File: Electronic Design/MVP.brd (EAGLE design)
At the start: 91.3 x 85.8 mm, 38 parts, among them IC1 ACS711KLCTR-12AB-T, IC3 ATMEGA328-PU, Q2 16MHz, Q3 IRF9540, Q4 IRF9540

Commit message: adding trace for pin16 on atmega to go to jumper
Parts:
- moved C3 46.4 mm to (78.5, 54.5), turned to 270 degrees
- moved C4 12.1 mm to (39.2, 42.5), turned to 270 degrees
- moved JP1 1.99 mm to (81.6, 44.9)
- moved Q2 1.99 mm to (85.2, 62.2)
- moved R1 1.99 mm to (73.5, 31.9)
- moved R5 1.99 mm to (79.5, 74.7)
- moved C13 1.99 mm to (85.3, 34.5)
- moved C20 1.99 mm to (78.5, 59.9)
- moved R3 1.99 mm to (44.6, 39.8)
- moved VIN_BUCK 1.99 mm to (76.1, 24.7)
- moved F1 1.99 mm to (29.0, 73.3)
- moved R12 1.99 mm to (18.6, 54.2)
- moved R14 1.99 mm to (30.7, 42.7)
- moved S1 1.99 mm to (28.9, 13.0)
- moved VIN 1.99 mm to (5.75, 70.2)
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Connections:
- net N$9: now also IC3.16
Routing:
- net +5V: track 119.3 -> 97.7 mm
- net GND: track 10.2 -> 0.00 mm
- net N$9: track 0.00 -> 8.11 mm
- net +3V3: track 106.3 -> 99.4 mm
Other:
- board size 91.3 x 85.8 mm -> 94.3 x 85.7 mm
- board text removed: "5V"
- board text removed: "GND"
- board text removed: "IIN1"
- board text removed: "VIN1"

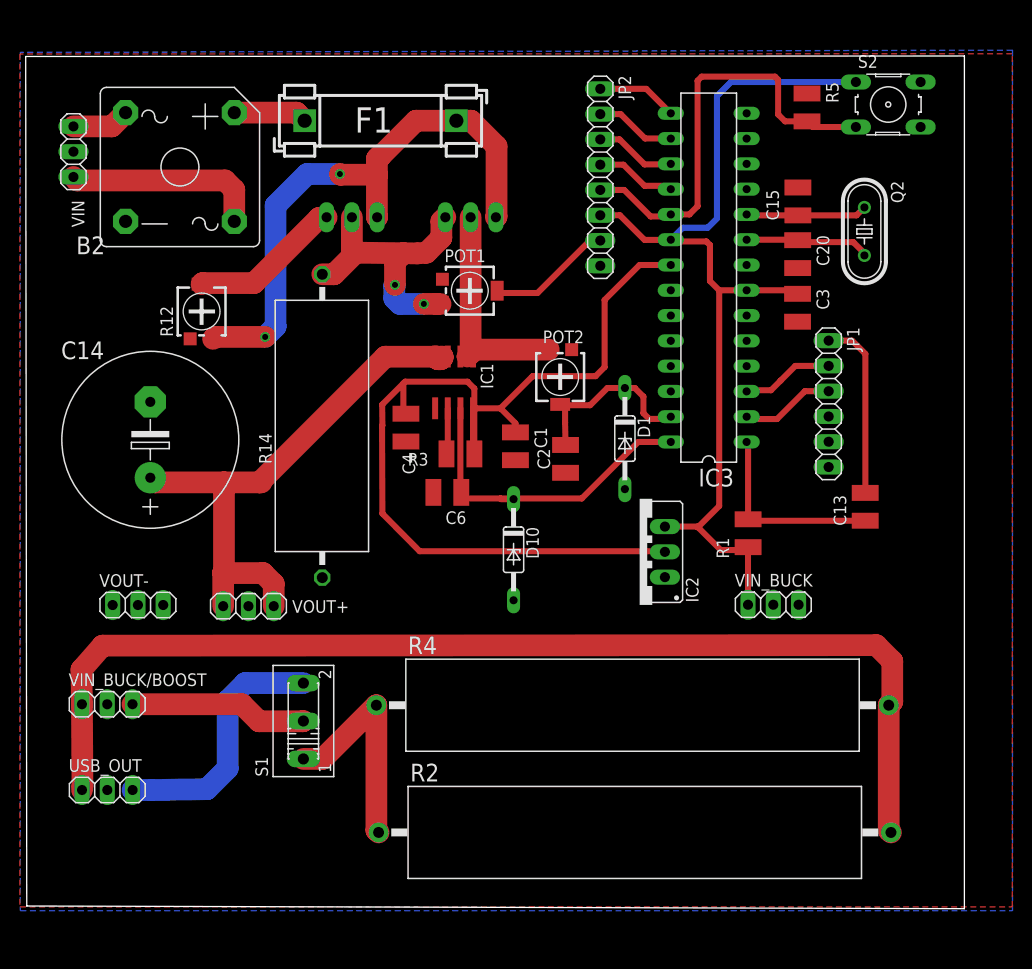
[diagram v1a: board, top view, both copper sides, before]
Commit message: Change some components connections in schematics and update board layout
changed top and bottom layer isolation to 0.3
completed unrouted wires
rerouted Output to come from capacitor directly
moved +3V3 near POT2 to allow more space forground trace to penetrate to C1 and C2
moved decoupling caps C4 and C1 closer to IC1 and IC3, respectively
added several ground stitching vias between top and bottom layer
increased some corner sizes
rerouted +5V from under IC4 to go through decoupling cap C3
connected R5 to GND
connected JP1 to GND
mirrored POT1 to allow easier routing
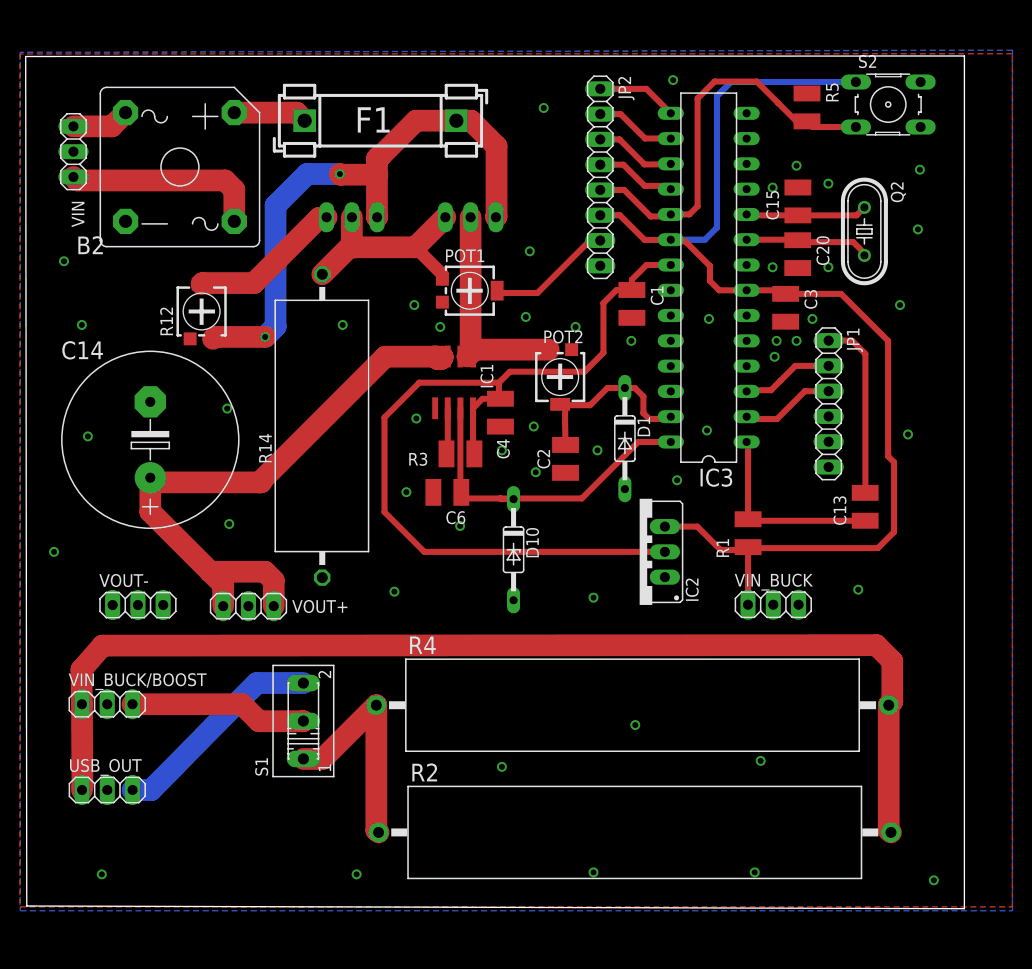
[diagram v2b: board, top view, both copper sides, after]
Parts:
- moved C1 18.5 mm to (61.9, 54.9)
- moved C4 9.62 mm to (48.7, 44.0)
- moved C3 1.20 mm to (77.3, 54.5)
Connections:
- removed net N$21: JP1.6
- removed net N$26: R5.1
- net GND: now also JP1.6, POT1.3, R5.1; no longer POT1.1
- net N$35: now also POT1.1; no longer POT1.3
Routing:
- net +5V: track 97.7 -> 118.1 mm
- net +3V3: track 99.4 -> 87.5 mm
- net N$35: track 29.2 -> 22.1 mm, vias 2 -> 0
- net M1S: track 56.6 -> 62.1 mm
- net N$25: track 25.6 -> 21.7 mm
- net N$8: track 44.1 -> 40.6 mm
- net IIN: track 31.9 -> 33.5 mm
- net VIN: track 18.0 -> 18.6 mm

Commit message: moved VOUT+, USB_OUT, VIN_BUCK/BOOST and VIN_BUCK closer to the edges as these will most likely be replaced with screw terminals (I couldn't find the component for these in eagle)
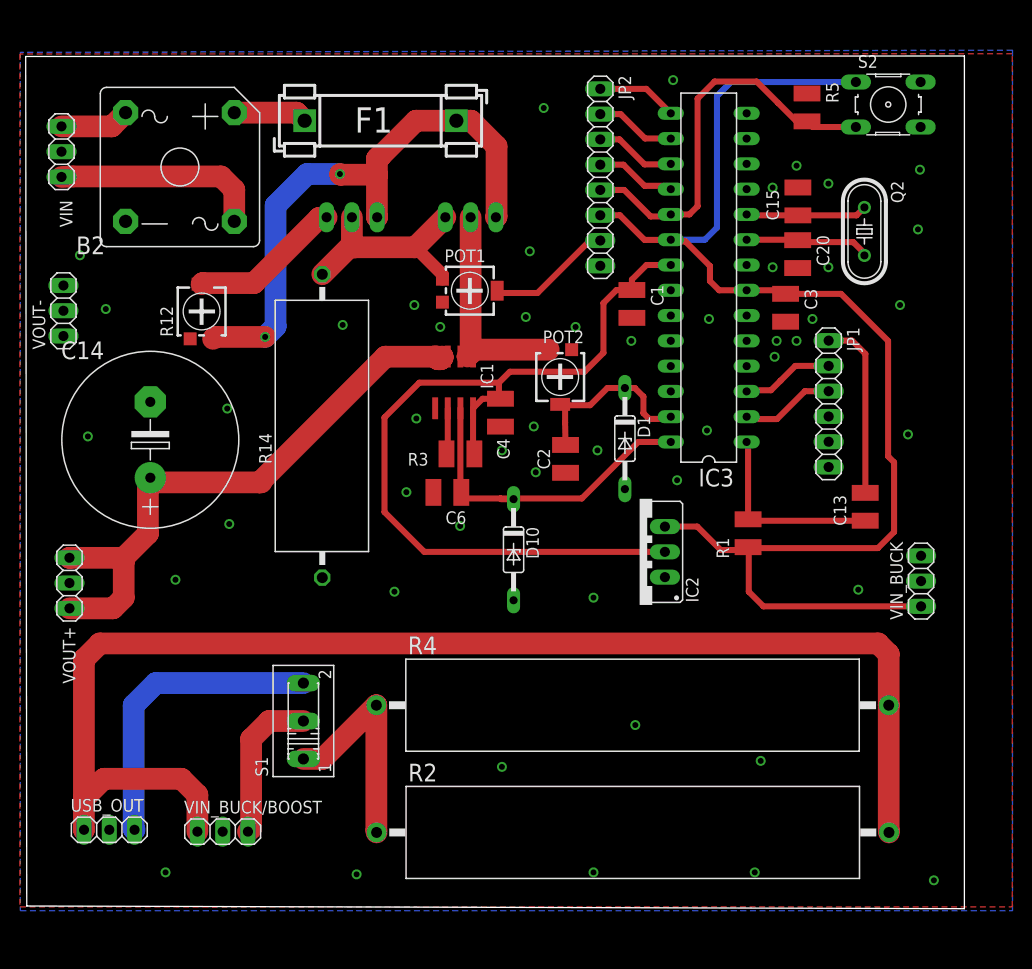
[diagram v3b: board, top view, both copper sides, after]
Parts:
- moved VOUT- 30.5 mm to (4.74, 54.2), turned to 90 degrees
- moved VOUT+ 18.1 mm to (5.35, 26.9), turned to 270 degrees
- moved VIN_BUCK/BOOST 17.3 mm to (20.7, 1.89)
- moved VIN_BUCK 15.0 mm to (90.9, 27.1), turned to 90 degrees
- moved USB_OUT 4.00 mm to (9.35, 2.07)
- moved VIN 1.20 mm to (4.55, 70.2)
- moved R2 0.20 mm to (61.9, 1.81)
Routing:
- net N$23: track 112.8 -> 133.6 mm
- net +5V: track 118.1 -> 134.7 mm
- net N$25: track 21.7 -> 30.5 mm
- net N$22: track 17.9 -> 15.4 mm
- net N$19: track 19.9 -> 21.1 mm
- net N$20: track 5.81 -> 7.01 mm
- net M1S: track 62.1 -> 61.2 mm

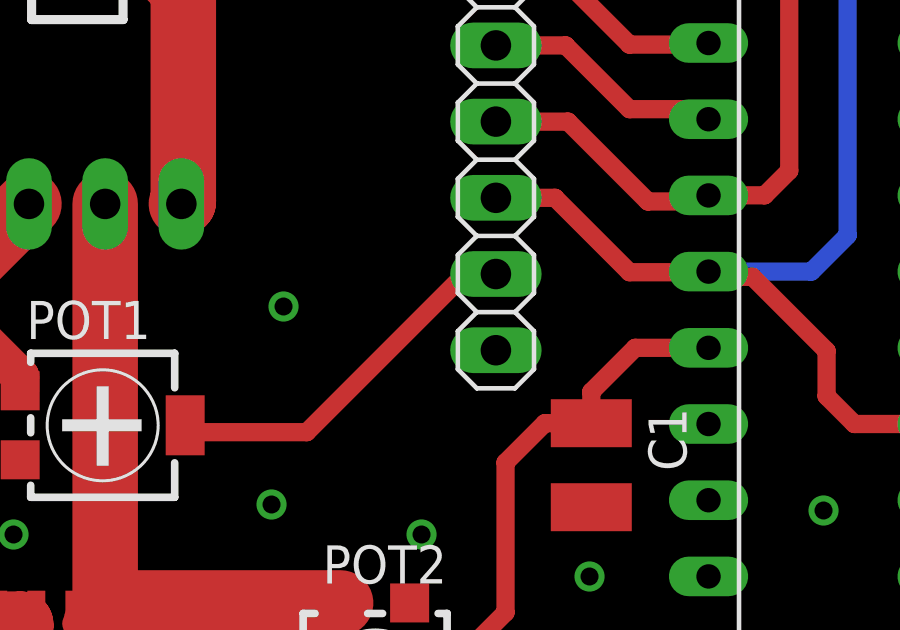
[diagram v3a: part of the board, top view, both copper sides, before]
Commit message: Changed position of 5V and overvoltage on JP2
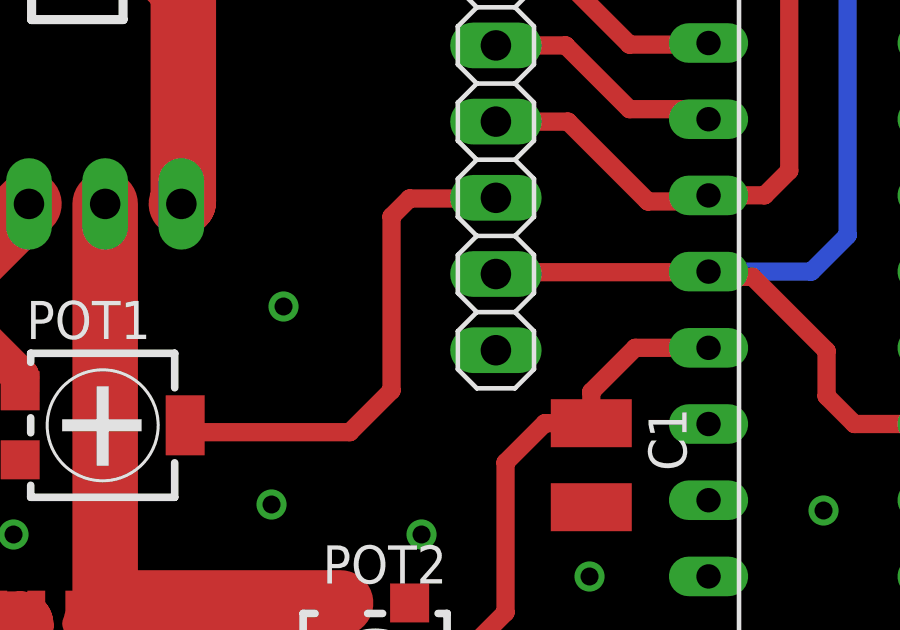
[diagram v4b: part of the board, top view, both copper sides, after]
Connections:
- net +5V: now also JP2.7; no longer JP2.6
- net OVERV: now also JP2.6; no longer JP2.7
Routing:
- net OVERV: track 12.6 -> 17.1 mm
- net +5V: track 134.7 -> 133.7 mm
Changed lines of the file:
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@@
 <wire x1="73.435846875" y1="30.3795" x2="73.532515625" y2="30.47616875" width="0.6096" layer="1"/>
 <contactref element="S2" pad="1"/>
-<contactref element="JP2" pad="6"/>
-<wire x1="58.67934375" y1="63.82278125" x2="60.65080625" y2="63.82278125" width="0.6096" layer="1"/>
-<wire x1="60.65080625" y1="63.82278125" x2="63.1309125" y2="61.342675" width="0.6096" layer="1"/>
-<wire x1="63.1309125" y1="61.342675" x2="65.746790625" y2="61.342675" width="0.6096" layer="1"/>
 <wire x1="65.746790625" y1="61.342675" x2="65.76684375" y2="61.362728125" width="0.6096" layer="1"/>
 <wire x1="84.36199375" y1="77.20865625" x2="71.811725" y2="77.20865625" width="0.6096" layer="16"/>
@@
 <wire x1="73.6" y1="26" x2="73.6" y2="30.408684375" width="0.6096" layer="1"/>
 <wire x1="73.6" y1="30.408684375" x2="73.532515625" y2="30.47616875" width="0.6096" layer="1"/>
+<contactref element="JP2" pad="7"/>
+<wire x1="65.746790625" y1="61.342675" x2="58.67934375" y2="61.342675" width="0.6096" layer="1"/>
+<wire x1="58.67934375" y1="61.342675" x2="58.67934375" y2="61.28278125" width="0.6096" layer="1"/>
 </signal>
 <signal name="N$1">
@@
 <signal name="OVERV">
 <contactref element="POT1" pad="2"/>
-<contactref element="JP2" pad="7"/>
-<wire x1="58.67934375" y1="61.28278125" x2="57.64759375" y2="61.28278125" width="0.6096" layer="1"/>
-<wire x1="57.64759375" y1="61.28278125" x2="52.375503125" y2="56.010690625" width="0.6096" layer="1"/>
-<wire x1="52.375503125" y1="56.010690625" x2="48.551171875" y2="56.010690625" width="0.6096" layer="1"/>
+<wire x1="53.810690625" y1="56.010690625" x2="48.551171875" y2="56.010690625" width="0.6096" layer="1"/>
 <wire x1="48.551171875" y1="56.010690625" x2="48.321371875" y2="56.240490625" width="0.6096" layer="1"/>
+<contactref element="JP2" pad="6"/>
+<wire x1="53.810690625" y1="56.010690625" x2="55.2" y2="57.4" width="0.6096" layer="1"/>
+<wire x1="55.2" y1="57.4" x2="55.2" y2="63.2" width="0.6096" layer="1"/>
+<wire x1="55.2" y1="63.2" x2="55.8" y2="63.8" width="0.6096" layer="1"/>
+<wire x1="55.8" y1="63.8" x2="58.6565625" y2="63.8" width="0.6096" layer="1"/>
+<wire x1="58.6565625" y1="63.8" x2="58.67934375" y2="63.82278125" width="0.6096" layer="1"/>
 </signal>
 </signals>

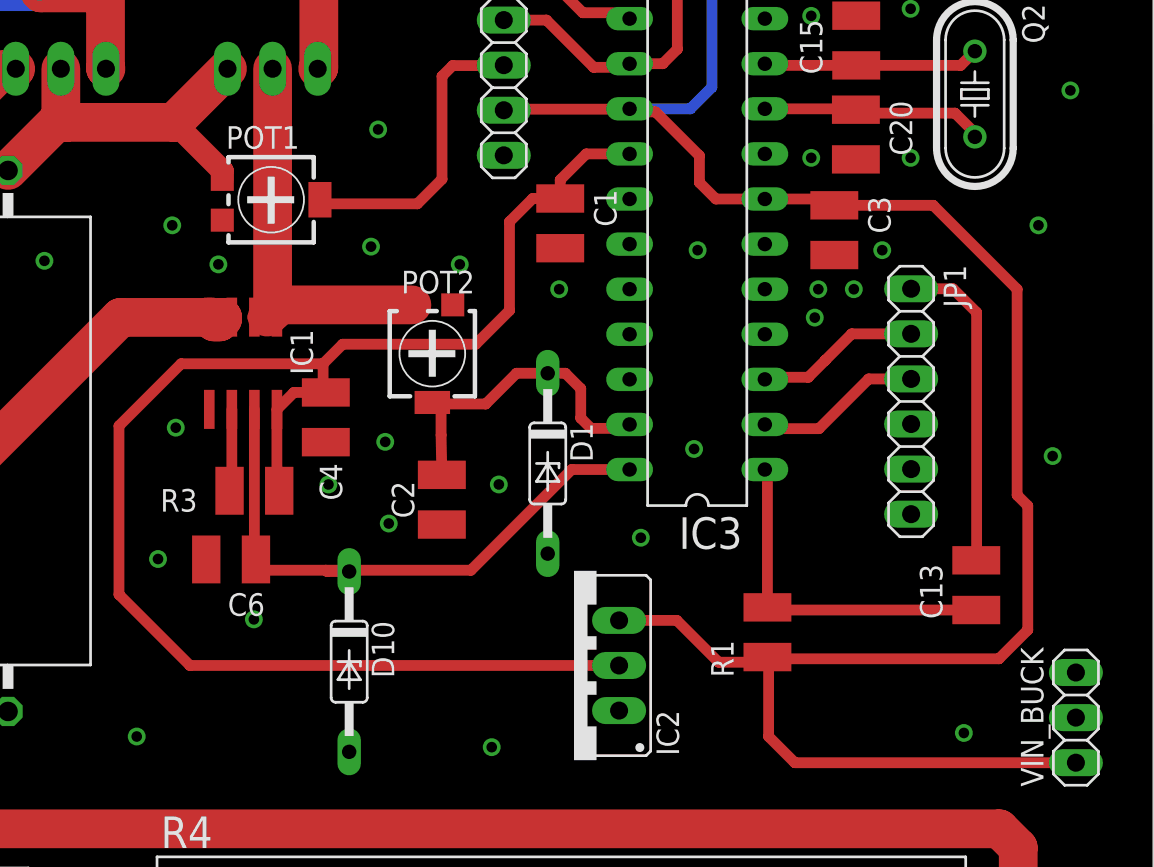
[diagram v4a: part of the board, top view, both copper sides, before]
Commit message: Updated circuit to reflect change from ACS711 to ACS712
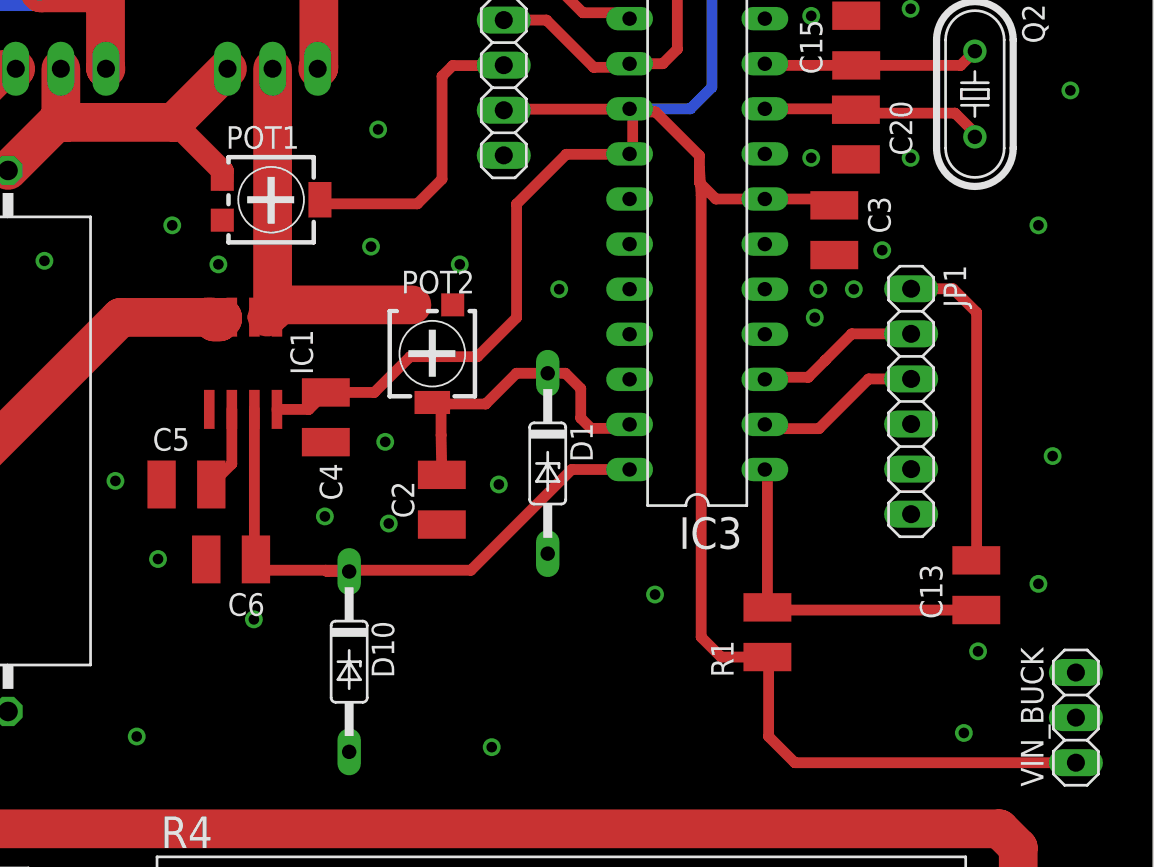
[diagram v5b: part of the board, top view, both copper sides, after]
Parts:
- removed C1: 10u, resistor:C1210
- removed IC2: (no value), v-reg:TO220S
- removed R3: 100k, resistor:R1210
- added C5: 1n, resistor:C1210
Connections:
- removed net +3V3: C1.1, C4.1, IC1.8, IC2.2, IC3.21, R3.1
- net +5V: now also C4.1, IC1.8, IC3.21; no longer IC2.3
- net GND: now also C5.1; no longer C1.2, IC2.1
- net N$2: now also C5.2; no longer R3.2
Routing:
- net +3V3: track 87.5 -> 0.00 mm
- net +5V: track 133.7 -> 140.2 mm

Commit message: Changing name of IC1 to reflect change of current sensing module
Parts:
- IC1: value ACS711KLCTR-12AB-T -> ACS712ELC-5A
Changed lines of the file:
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@@
 <attribute name="VALUE" x="47.37079375" y="29.963215625" size="1.27" layer="27" ratio="10" rot="R270"/>
 </element>
-<element name="IC1" library="mylibrary" package="SOIC8" value="ACS711KLCTR-12AB-T" x="43.9929625" y="47.0281875" smashed="yes" rot="R180">
+<element name="IC1" library="mylibrary" package="SOIC8" value="ACS712ELC-5A" x="43.9929625" y="47.0281875" smashed="yes" rot="R180">
 <attribute name="NAME" x="46.6599625" y="48.9331875" size="1.27" layer="25" rot="R270"/>
 <attribute name="VALUE" x="34.898875" y="50.4118" size="1.27" layer="27"/>
